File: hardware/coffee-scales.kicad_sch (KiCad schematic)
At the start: 6 parts, among them J1 Conn_01x04, SW1 SW_Push, U1 Adafruit_Feather_328P, U2 HX711_Breakout, U3 4DIGIT_7SEG, U4 4DIGIT_7SEG

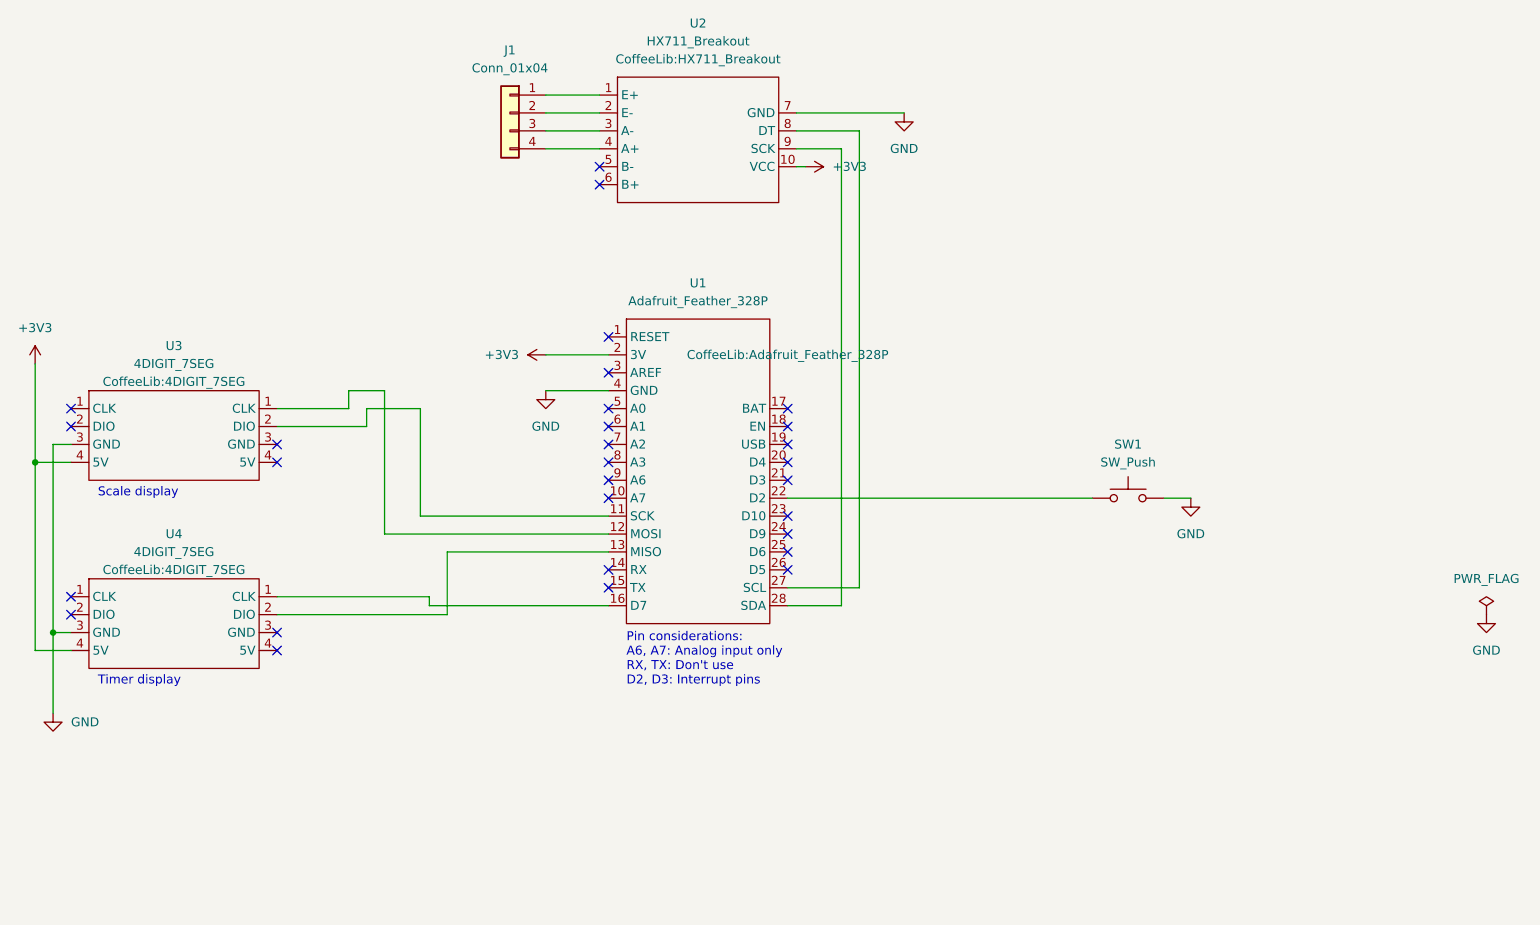
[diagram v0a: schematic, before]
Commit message: Clean up schematic a bit
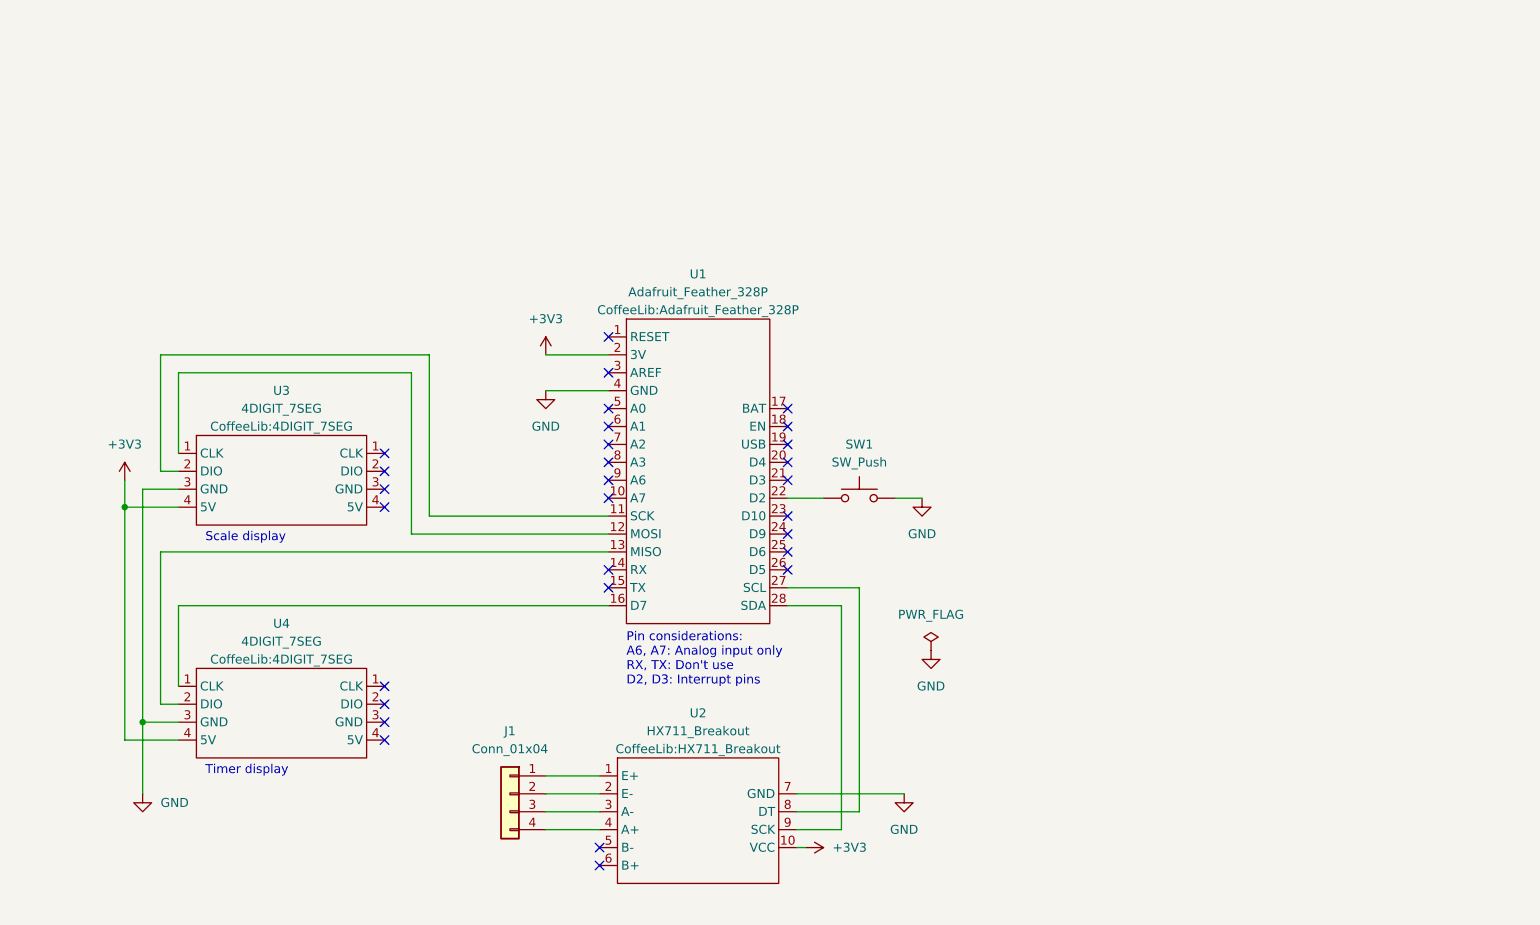
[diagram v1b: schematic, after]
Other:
- moved on the sheet: J1, SW1, U2, U3, U4

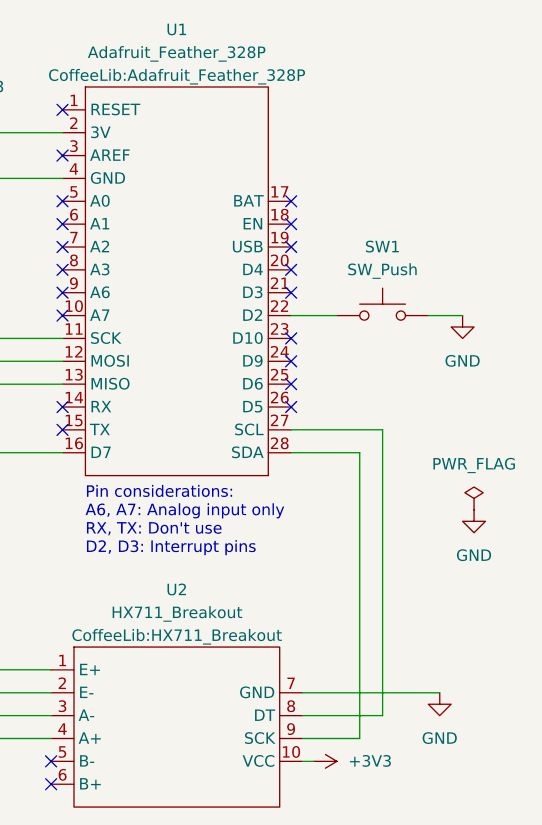
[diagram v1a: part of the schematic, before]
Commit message: Wire button and HX711 DT to interrupt pins
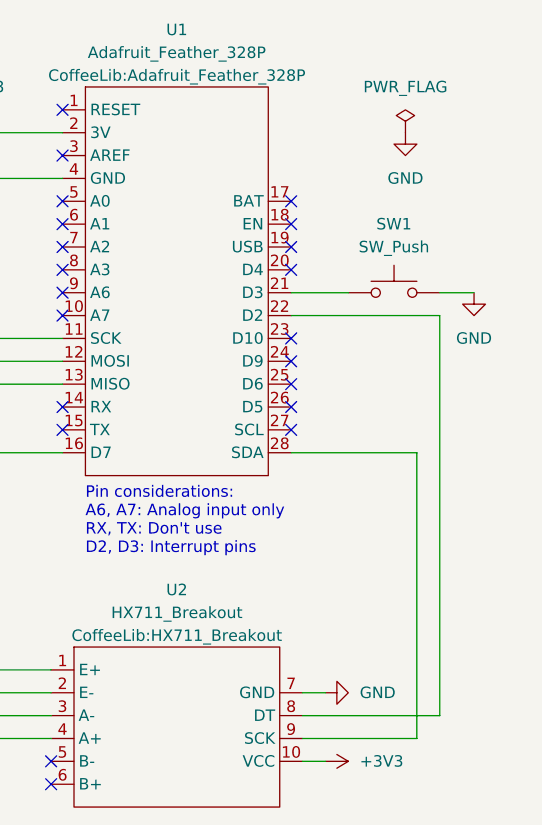
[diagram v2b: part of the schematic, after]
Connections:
- net at SW1.1: now also U1.21 (D3); no longer U1.22 (D2)
- net at U2.8 (DT): now also U1.22 (D2); no longer U1.27 (SCL)
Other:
- moved on the sheet: SW1
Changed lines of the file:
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@@
   (no_connect (at 119.38 96.52))
   (no_connect (at 144.78 101.6))
-  (no_connect (at 144.78 104.14))
   (no_connect (at 144.78 93.98))
   (no_connect (at 144.78 96.52))
@@
   (no_connect (at 118.11 156.21))
   (no_connect (at 118.11 158.75))
-  (wire (pts (xy 146.05 148.59) (xy 161.29 148.59))
-    (stroke (width 0) (type default) (color 0 0 0 0))
-  )
-  (wire (pts (xy 146.05 151.13) (xy 154.94 151.13))
-    (stroke (width 0) (type default) (color 0 0 0 0))
-  )
-  (wire (pts (xy 152.4 121.92) (xy 144.78 121.92))
+  (no_connect (at 144.78 119.38))
+  (wire (pts (xy 146.05 151.13) (xy 161.29 151.13))
+    (stroke (width 0) (type default) (color 0 0 0 0))
+  )
+  (wire (pts (xy 158.75 121.92) (xy 144.78 121.92))
     (stroke (width 0) (type default) (color 0 0 0 0))
   )
@@
     (stroke (width 0) (type default) (color 0 0 0 0))
   )
+  (wire (pts (xy 144.78 104.14) (xy 151.13 104.14))
+    (stroke (width 0) (type default) (color 0 0 0 0))
+  )
   (wire (pts (xy 50.8 107.95) (xy 58.42 107.95))
     (stroke (width 0) (type default) (color 0 0 0 0))
@@
     (stroke (width 0) (type default) (color 0 0 0 0))
   )
-  (wire (pts (xy 163.83 106.68) (xy 160.02 106.68))
+  (wire (pts (xy 165.1 104.14) (xy 161.29 104.14))
     (stroke (width 0) (type default) (color 0 0 0 0))
   )
@@
     (stroke (width 0) (type default) (color 0 0 0 0))
   )
-  (wire (pts (xy 144.78 106.68) (xy 149.86 106.68))
+  (wire (pts (xy 144.78 106.68) (xy 161.29 106.68))
     (stroke (width 0) (type default) (color 0 0 0 0))
   )
@@
     (stroke (width 0) (type default) (color 0 0 0 0))
   )
-  (wire (pts (xy 146.05 153.67) (xy 152.4 153.67))
+  (wire (pts (xy 146.05 153.67) (xy 158.75 153.67))
     (stroke (width 0) (type default) (color 0 0 0 0))
   )
@@
     (stroke (width 0) (type default) (color 0 0 0 0))
   )
-  (wire (pts (xy 154.94 119.38) (xy 144.78 119.38))
+  (wire (pts (xy 161.29 106.68) (xy 161.29 151.13))
     (stroke (width 0) (type default) (color 0 0 0 0))
   )
@@
     (stroke (width 0) (type default) (color 0 0 0 0))
   )
+  (wire (pts (xy 146.05 148.59) (xy 148.59 148.59))
+    (stroke (width 0) (type default) (color 0 0 0 0))
+  )
   (wire (pts (xy 55.88 102.87) (xy 58.42 102.87))
     (stroke (width 0) (type default) (color 0 0 0 0))
@@
     (stroke (width 0) (type default) (color 0 0 0 0))
   )
-  (wire (pts (xy 152.4 153.67) (xy 152.4 121.92))
-    (stroke (width 0) (type default) (color 0 0 0 0))
-  )
-  (wire (pts (xy 146.05 156.21) (xy 147.32 156.21))
+  (wire (pts (xy 158.75 153.67) (xy 158.75 121.92))
+    (stroke (width 0) (type default) (color 0 0 0 0))
+  )
+  (wire (pts (xy 146.05 156.21) (xy 148.59 156.21))
     (stroke (width 0) (type default) (color 0 0 0 0))
   )
@@
   )
   (wire (pts (xy 55.88 135.89) (xy 58.42 135.89))
-    (stroke (width 0) (type default) (color 0 0 0 0))
-  )
-  (wire (pts (xy 154.94 151.13) (xy 154.94 119.38))
     (stroke (width 0) (type default) (color 0 0 0 0))
   )
@@
     (effects (font (size 1.27 1.27)) (justify left bottom))
   )
-  (symbol (lib_id "Switch:SW_Push") (at 154.94 106.68 0) (unit 1)
+  (symbol (lib_id "Switch:SW_Push") (at 156.21 104.14 0) (unit 1)
     (in_bom yes) (on_board yes)
-    (property "Reference" "SW1" (id 0) (at 154.94 99.06 0))
-    (property "Value" "SW_Push" (id 1) (at 154.94 101.6 0))
-    (property "Footprint" "Button_Switch_THT:SW_PUSH-12mm" (id 2) (at 154.94 109.22 0)
-      (effects (font (size 1.27 1.27)) hide)
-    )
-    (property "Datasheet" "~" (id 3) (at 154.94 101.6 0)
-      (effects (font (size 1.27 1.27)) hide)
-    )
-    (pin "1")
-    (pin "2")
-  )
-  (symbol (lib_id "power:+3V3") (at 147.32 156.21 270) (unit 1)
-    (in_bom yes) (on_board yes) (fields_autoplaced)
-    (property "Reference" "#PWR06" (id 0) (at 143.51 156.21 0)
-      (effects (font (size 1.27 1.27)) hide)
-    )
-    (property "Value" "+3V3" (id 1) (at 151.13 156.2099 90)
+    (property "Reference" "SW1" (id 0) (at 156.21 96.52 0))
+    (property "Value" "SW_Push" (id 1) (at 156.21 99.06 0))
+    (property "Footprint" "Button_Switch_THT:SW_PUSH-12mm" (id 2) (at 156.21 106.68 0)
+      (effects (font (size 1.27 1.27)) hide)
+    )
+    (property "Datasheet" "~" (id 3) (at 156.21 99.06 0)
+      (effects (font (size 1.27 1.27)) hide)
+    )
+    (pin "1")
+    (pin "2")
+  )
+  (symbol (lib_id "power:+3V3") (at 148.59 156.21 270) (unit 1)
+    (in_bom yes) (on_board yes) (fields_autoplaced)
+    (property "Reference" "#PWR06" (id 0) (at 144.78 156.21 0)
+      (effects (font (size 1.27 1.27)) hide)
+    )
+    (property "Value" "+3V3" (id 1) (at 152.4 156.2099 90)
       (effects (font (size 1.27 1.27)) (justify left))
     )
-    (property "Footprint" "" (id 2) (at 147.32 156.21 0)
-      (effects (font (size 1.27 1.27)) hide)
-    )
-    (property "Datasheet" "" (id 3) (at 147.32 156.21 0)
+    (property "Footprint" "" (id 2) (at 148.59 156.21 0)
+      (effects (font (size 1.27 1.27)) hide)
+    )
+    (property "Datasheet" "" (id 3) (at 148.59 156.21 0)
       (effects (font (size 1.27 1.27)) hide)
     )
@@
     (pin "9")
   )
-  (symbol (lib_id "power:GND") (at 161.29 148.59 0) (unit 1)
-    (in_bom yes) (on_board yes) (fields_autoplaced)
-    (property "Reference" "#PWR07" (id 0) (at 161.29 154.94 0)
-      (effects (font (size 1.27 1.27)) hide)
-    )
-    (property "Value" "GND" (id 1) (at 161.29 153.67 0))
-    (property "Footprint" "" (id 2) (at 161.29 148.59 0)
-      (effects (font (size 1.27 1.27)) hide)
-    )
-    (property "Datasheet" "" (id 3) (at 161.29 148.59 0)
+  (symbol (lib_id "power:GND") (at 148.59 148.59 90) (unit 1)
+    (in_bom yes) (on_board yes) (fields_autoplaced)
+    (property "Reference" "#PWR07" (id 0) (at 154.94 148.59 0)
+      (effects (font (size 1.27 1.27)) hide)
+    )
+    (property "Value" "GND" (id 1) (at 152.4 148.5899 90)
+      (effects (font (size 1.27 1.27)) (justify right))
+    )
+    (property "Footprint" "" (id 2) (at 148.59 148.59 0)
+      (effects (font (size 1.27 1.27)) hide)
+    )
+    (property "Datasheet" "" (id 3) (at 148.59 148.59 0)
       (effects (font (size 1.27 1.27)) hide)
     )
@@
   (symbol (lib_id "power:+3V3") (at 110.49 86.36 0) (unit 1)
     (in_bom yes) (on_board yes) (fields_autoplaced)
-    (property "Reference" "#PWR?" (id 0) (at 110.49 90.17 0)
+    (property "Reference" "#PWR0101" (id 0) (at 110.49 90.17 0)
       (effects (font (size 1.27 1.27)) hide)
     )
@@
     (pin "1")
   )
-  (symbol (lib_id "power:GND") (at 165.1 128.27 0) (unit 1)
-    (in_bom yes) (on_board yes) (fields_autoplaced)
-    (property "Reference" "#PWR010" (id 0) (at 165.1 134.62 0)
-      (effects (font (size 1.27 1.27)) hide)
-    )
-    (property "Value" "GND" (id 1) (at 165.1 133.35 0))
-    (property "Footprint" "" (id 2) (at 165.1 128.27 0)
-      (effects (font (size 1.27 1.27)) hide)
-    )
-    (property "Datasheet" "" (id 3) (at 165.1 128.27 0)
+  (symbol (lib_id "power:GND") (at 157.48 86.36 0) (unit 1)
+    (in_bom yes) (on_board yes) (fields_autoplaced)
+    (property "Reference" "#PWR010" (id 0) (at 157.48 92.71 0)
+      (effects (font (size 1.27 1.27)) hide)
+    )
+    (property "Value" "GND" (id 1) (at 157.48 91.44 0))
+    (property "Footprint" "" (id 2) (at 157.48 86.36 0)
+      (effects (font (size 1.27 1.27)) hide)
+    )
+    (property "Datasheet" "" (id 3) (at 157.48 86.36 0)
       (effects (font (size 1.27 1.27)) hide)
     )
@@
     (pin "4")
   )
-  (symbol (lib_id "power:PWR_FLAG") (at 165.1 128.27 0) (unit 1)
-    (in_bom yes) (on_board yes) (fields_autoplaced)
-    (property "Reference" "#FLG01" (id 0) (at 165.1 126.365 0)
-      (effects (font (size 1.27 1.27)) hide)
-    )
-    (property "Value" "PWR_FLAG" (id 1) (at 165.1 123.19 0))
-    (property "Footprint" "" (id 2) (at 165.1 128.27 0)
-      (effects (font (size 1.27 1.27)) hide)
-    )
-    (property "Datasheet" "~" (id 3) (at 165.1 128.27 0)
+  (symbol (lib_id "power:PWR_FLAG") (at 157.48 86.36 0) (unit 1)
+    (in_bom yes) (on_board yes) (fields_autoplaced)
+    (property "Reference" "#FLG01" (id 0) (at 157.48 84.455 0)
+      (effects (font (size 1.27 1.27)) hide)
+    )
+    (property "Value" "PWR_FLAG" (id 1) (at 157.48 81.28 0))
+    (property "Footprint" "" (id 2) (at 157.48 86.36 0)
+      (effects (font (size 1.27 1.27)) hide)
+    )
+    (property "Datasheet" "~" (id 3) (at 157.48 86.36 0)
       (effects (font (size 1.27 1.27)) hide)
     )
@@
     (pin "9")
   )
-  (symbol (lib_id "power:GND") (at 163.83 106.68 0) (unit 1)
-    (in_bom yes) (on_board yes) (fields_autoplaced)
-    (property "Reference" "#PWR05" (id 0) (at 163.83 113.03 0)
-      (effects (font (size 1.27 1.27)) hide)
-    )
-    (property "Value" "GND" (id 1) (at 163.83 111.76 0))
-    (property "Footprint" "" (id 2) (at 163.83 106.68 0)
-      (effects (font (size 1.27 1.27)) hide)
-    )
-    (property "Datasheet" "" (id 3) (at 163.83 106.68 0)
+  (symbol (lib_id "power:GND") (at 165.1 104.14 0) (unit 1)
+    (in_bom yes) (on_board yes) (fields_autoplaced)
+    (property "Reference" "#PWR05" (id 0) (at 165.1 110.49 0)
+      (effects (font (size 1.27 1.27)) hide)
+    )
+    (property "Value" "GND" (id 1) (at 165.1 109.22 0))
+    (property "Footprint" "" (id 2) (at 165.1 104.14 0)
+      (effects (font (size 1.27 1.27)) hide)
+    )
+    (property "Datasheet" "" (id 3) (at 165.1 104.14 0)
       (effects (font (size 1.27 1.27)) hide)
     )
@@
     )
     (path "/282afdc6-7b29-4f18-87e4-ee8540aff3f2"
-      (reference "#PWR?") (unit 1) (value "+3V3") (footprint "")
+      (reference "#PWR0101") (unit 1) (value "+3V3") (footprint "")
     )
     (path "/b847d4fb-00a9-4e1e-95a6-5b5c153c00bf"
